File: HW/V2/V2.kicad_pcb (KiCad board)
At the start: 2 copper layers, 107.1 x 66 mm, 80 parts, among them J2 +24VDC, J3 USB_B_Mini, J4 +7.5VDC, Q1 Si4435, Q2 BSS138, Q3 Si4435, Q4 BSS138, Q5 BSS138, U1 MAX6126_50, U10 74HCT2G14GV, U12 AD8221, U13 ADS1115-DIP, U14 OLED_128x64_SPI_0.96, U2 AP2210-3.3V, U3 Bluepill, U4 DS2401Z, U5 DS2401Z, U6 AD8221, U8 CH340G, U9 M24C01-WMN, Y1 12MHZ

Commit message: V2 milling and BOM
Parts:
- removed C18: 10uF, Capacitor_Tantalum_SMD:CP_EIA-3528-12_Kemet-T_Pad1.50x2.35mm_HandSolder
- removed C19: CP_Small, Capacitor_Tantalum_SMD:CP_EIA-3528-12_Kemet-T_Pad1.50x2.35mm_HandSolder
- removed C36: 1000uF50V, Capacitor_THT:CP_Radial_D16.0mm_P7.50mm
- removed J2: +24VDC, TerminalBlock_MetzConnect:TerminalBlock_MetzConnect_Type175_RT02702HBLC_1x02_P7.50mm_Horizontal
- removed J4: +7.5VDC, TerminalBlock:TerminalBlock_bornier-2_P5.08mm
- removed R20: 1K5-5K, Resistor_SMD:R_0805_2012Metric_Pad1.15x1.40mm_HandSolder
- removed TP1: VrefTest, TestPoint:TestPoint_Loop_D2.50mm_Drill1.0mm
- removed U4: DS2401Z, Package_TO_SOT_SMD:SOT-223
- added C6: 68uf, Capacitor_SMD:C_1210_3225Metric_Pad1.42x2.65mm_HandSolder, B.Cu at (127.3, 60.7)
- added U15: +7.5VDC, Libs:Conn_Microfit_Vertical_molex, B.Cu at (138.9, 88.1)
- added U7: +24VDC, Libs:Conn_Microfit_Vertical_molex, B.Cu at (128.1, 96.4)
- C1: value 68uf -> 100N; footprint Capacitor_SMD:C_1210_3225Metric_Pad1.42x2.65mm_HandSolder -> Capacitor_SMD:C_0805_2012Metric_Pad1.15x1.40mm_HandSolder
- C12, C13, C20, C21, C29, C30, C5, C7, D1, J3, R1, R10, R13, R14, R15, R16, R24, R25, R4, R5, U10, U2, U8, Y1: moved to B.Cu
- C16, Q2, Q4: moved to F.Cu
- R30: value 1K -> 2K
- R31: value 2K -> 10K
- moved C2 195.4 mm to (97.5, 75.7), turned to 270 degrees
- moved C1 190.5 mm to (103.4, 72.6)
- moved C4 172.0 mm to (114.0, 72.1)
- moved C3 172.0 mm to (114.0, 74.2)
- moved C5 161.0 mm to (136.1, 98.3), turned to 270 degrees
- moved U2 152.0 mm to (139.4, 98.8), turned to 270 degrees
- moved C7 140.9 mm to (143.0, 99.1), turned to 90 degrees
- moved R1 139.3 mm to (153.2, 62.2), turned to 180 degrees
- moved C8 135.1 mm to (137.9, 96.8), turned to 90 degrees
- moved C28 129.6 mm to (200.7, 55.1), turned to 90 degrees
- moved C13 126.5 mm to (153.7, 93.5)
- moved R17 114.3 mm to (170.4, 75.7)
- moved C14 111.6 mm to (182.1, 62.7), turned to 180 degrees
- moved C20 105.5 mm to (190.5, 86.6), turned to 180 degrees
- moved C12 104.8 mm to (177.3, 62.7)
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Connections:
- C1 pad 1: Net-(C1-Pad1) -> +7.5V
- C2 pad 1: Net-(C1-Pad1) -> Net-(C2-Pad1)
- R21 pad 2: /Power/oneWireTemp -> /MCU/MOSFETtemp
- U1 pad 1: Net-(C1-Pad1) -> Net-(C2-Pad1)
- U3 pad 13: /Power/oneWireTemp -> Net-(U3-Pad13)
- U5 pad 1: /Power/oneWireTemp -> /MCU/MOSFETtemp
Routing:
- net +3V3: track 0.00 -> 488.8 mm, vias 0 -> 6
- net GND: track 0.00 -> 461.9 mm, vias 0 -> 11
- net /MCU/SCL: track 0.00 -> 126.2 mm, vias 0 -> 2
- net /MCU/SDA: track 0.00 -> 111.8 mm, vias 0 -> 2
- net +5vREF: track 0.00 -> 79.8 mm, vias 0 -> 3
- net +7.5V: track 0.00 -> 79.6 mm, vias 0 -> 1
- net CS: track 0.00 -> 70.0 mm, vias 0 -> 2
- net BTN_DN: track 0.00 -> 66.4 mm, vias 0 -> 2
- net BTN_UP: track 0.00 -> 61.0 mm, vias 0 -> 2
- net Net-(SW1-Pad1): track 0.00 -> 56.9 mm, vias 0 -> 2
- net SCK: track 0.00 -> 54.9 mm
- net Net-(Q4-Pad3): track 0.00 -> 54.2 mm, vias 0 -> 1
- net MOSI: track 0.00 -> 50.9 mm
- net Net-(Q2-Pad3): track 3.73 -> 51.3 mm, vias 0 -> 1
- net RESET: track 0.00 -> 44.9 mm
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
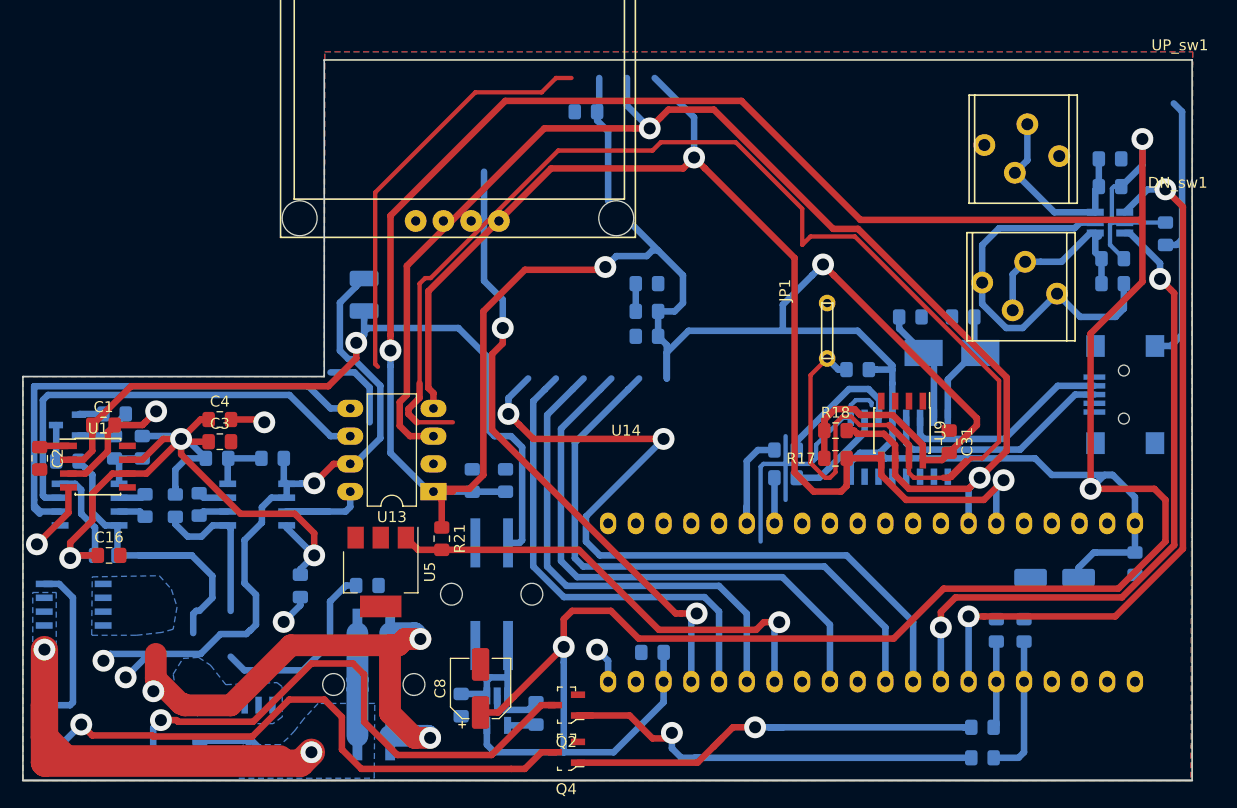
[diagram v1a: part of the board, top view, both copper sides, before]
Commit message: piggyback ADC amp
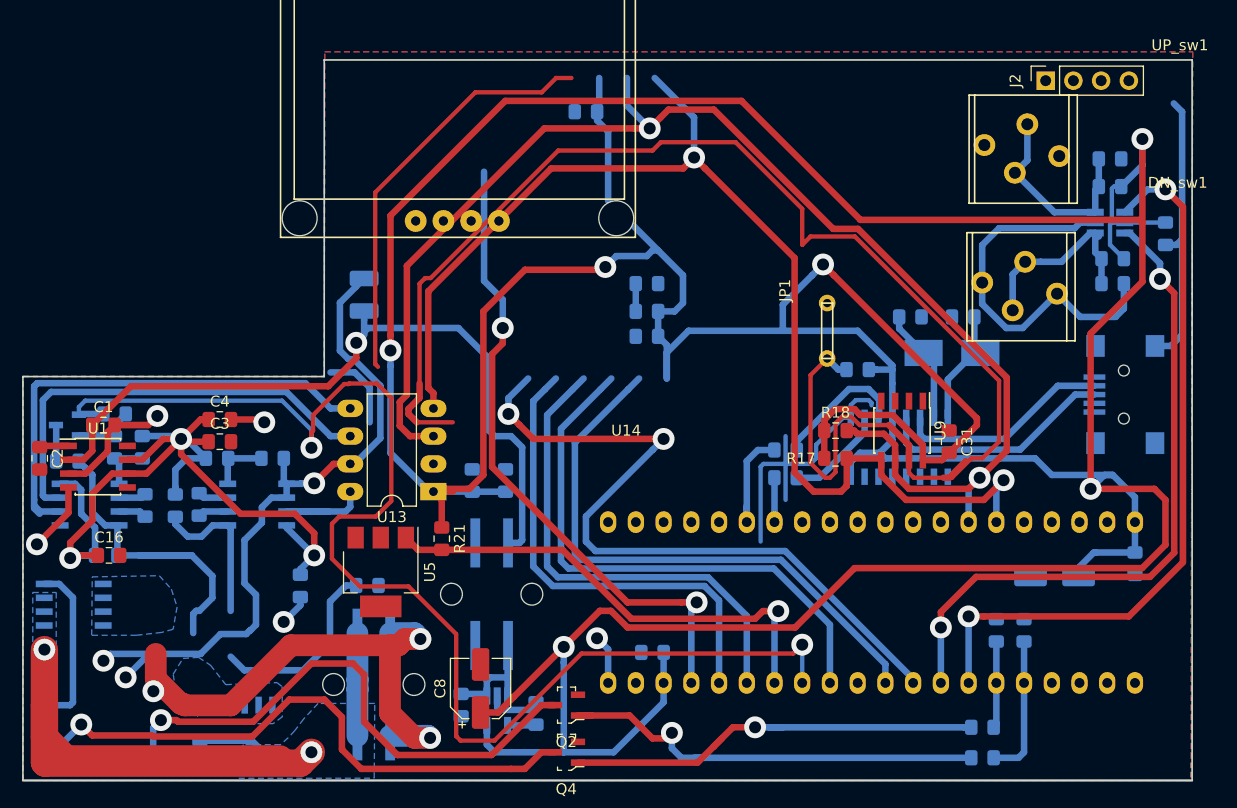
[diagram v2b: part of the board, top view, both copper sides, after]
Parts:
- added J2: I2CHeader, Connector_PinSocket_2.54mm:PinSocket_1x04_P2.54mm_Vertical, F.Cu at (189.7, 41.1)
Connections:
- Q5 pad 1: /Temperature mangement/WMRTresistorDivider -> /MCU/WMRTresistorDivider
- R31 pad 1: /Temperature mangement/WMRTresistorDivider -> /MCU/WMRTresistorDivider
- U3 pad 13: Net-(U3-Pad13) -> /MCU/WMRTresistorDivider
- U5 pad 1: /MCU/MOSFETtemp -> Net-(U5-Pad1)
- U5 pad 2: GND -> Net-(U5-Pad2)
- U5 pad 3: (no net) -> Net-(U5-Pad3)
- U5 pad 4: GND -> Net-(U5-Pad2)
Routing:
- net /MCU/WMRTresistorDivider: track 0.00 -> 120.7 mm, vias 0 -> 2
- net CS: track 70.0 -> 66.9 mm
- net Net-(SW1-Pad1): track 56.9 -> 59.5 mm
- net /Temperature mangement/WMRTresistorDivider: track 2.27 -> 0.00 mm
- net +3V3: track 488.8 -> 486.7 mm
- net SCK: track 54.9 -> 53.0 mm
- net GND: track 461.9 -> 463.1 mm
- net BTN_DN: track 66.4 -> 67.1 mm
- net AO: track 43.2 -> 43.8 mm
